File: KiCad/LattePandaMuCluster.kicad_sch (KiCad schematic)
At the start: 0 parts

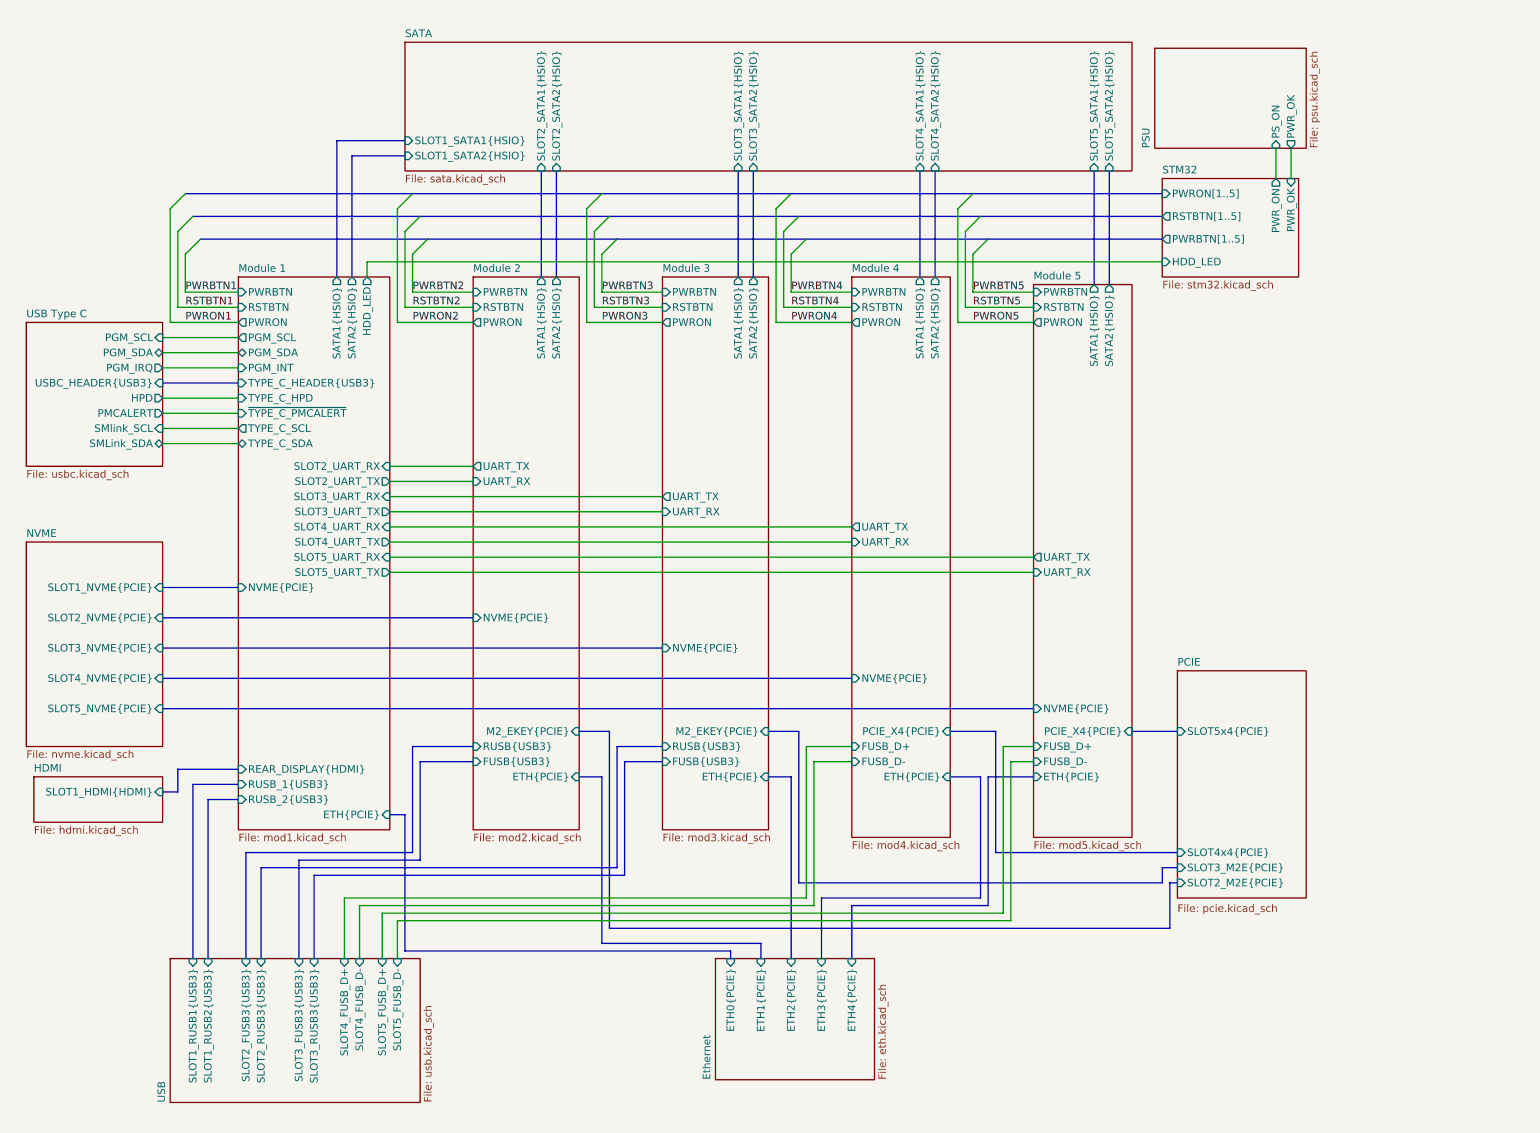
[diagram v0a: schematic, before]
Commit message: Add m.2 slot footprints
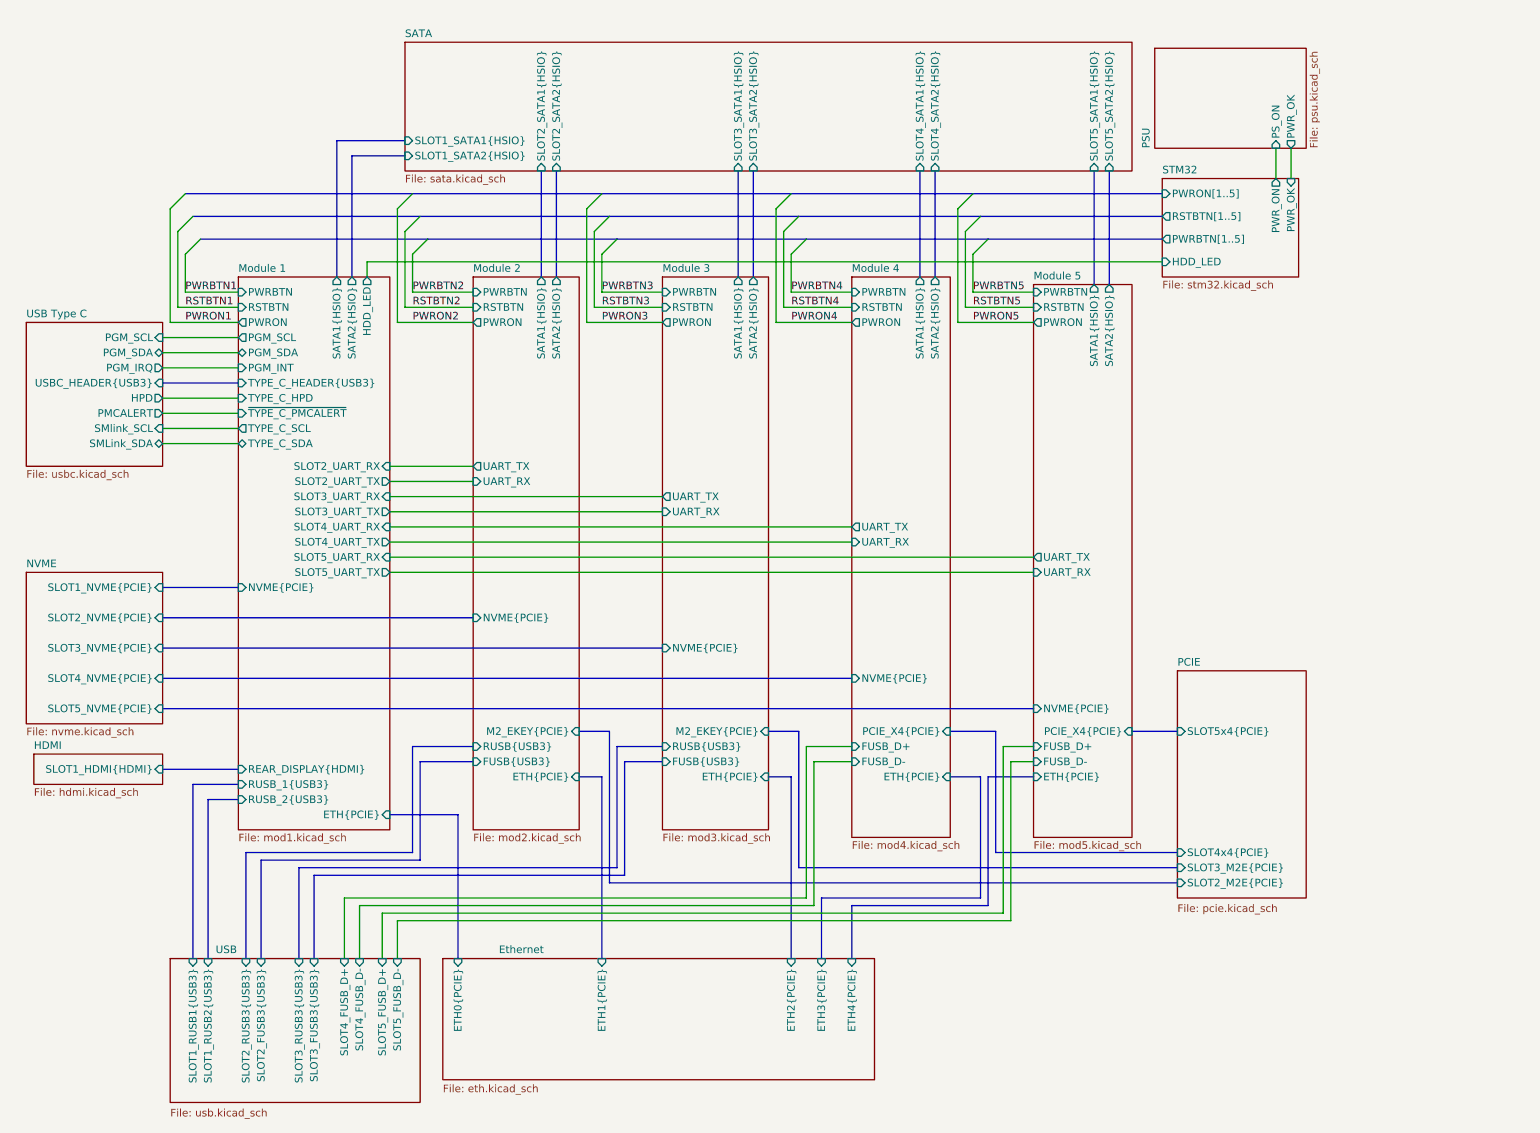
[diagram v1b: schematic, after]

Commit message: Finish fixing footprints
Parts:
- added H1, H2, H3, H4: MountingHole_Pad, MountingHole:MountingHole_4mm_Pad_Via, symbol Mechanical:MountingHole_Pad
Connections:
- new net GND: H1.1, H2.1, H3.1, H4.1

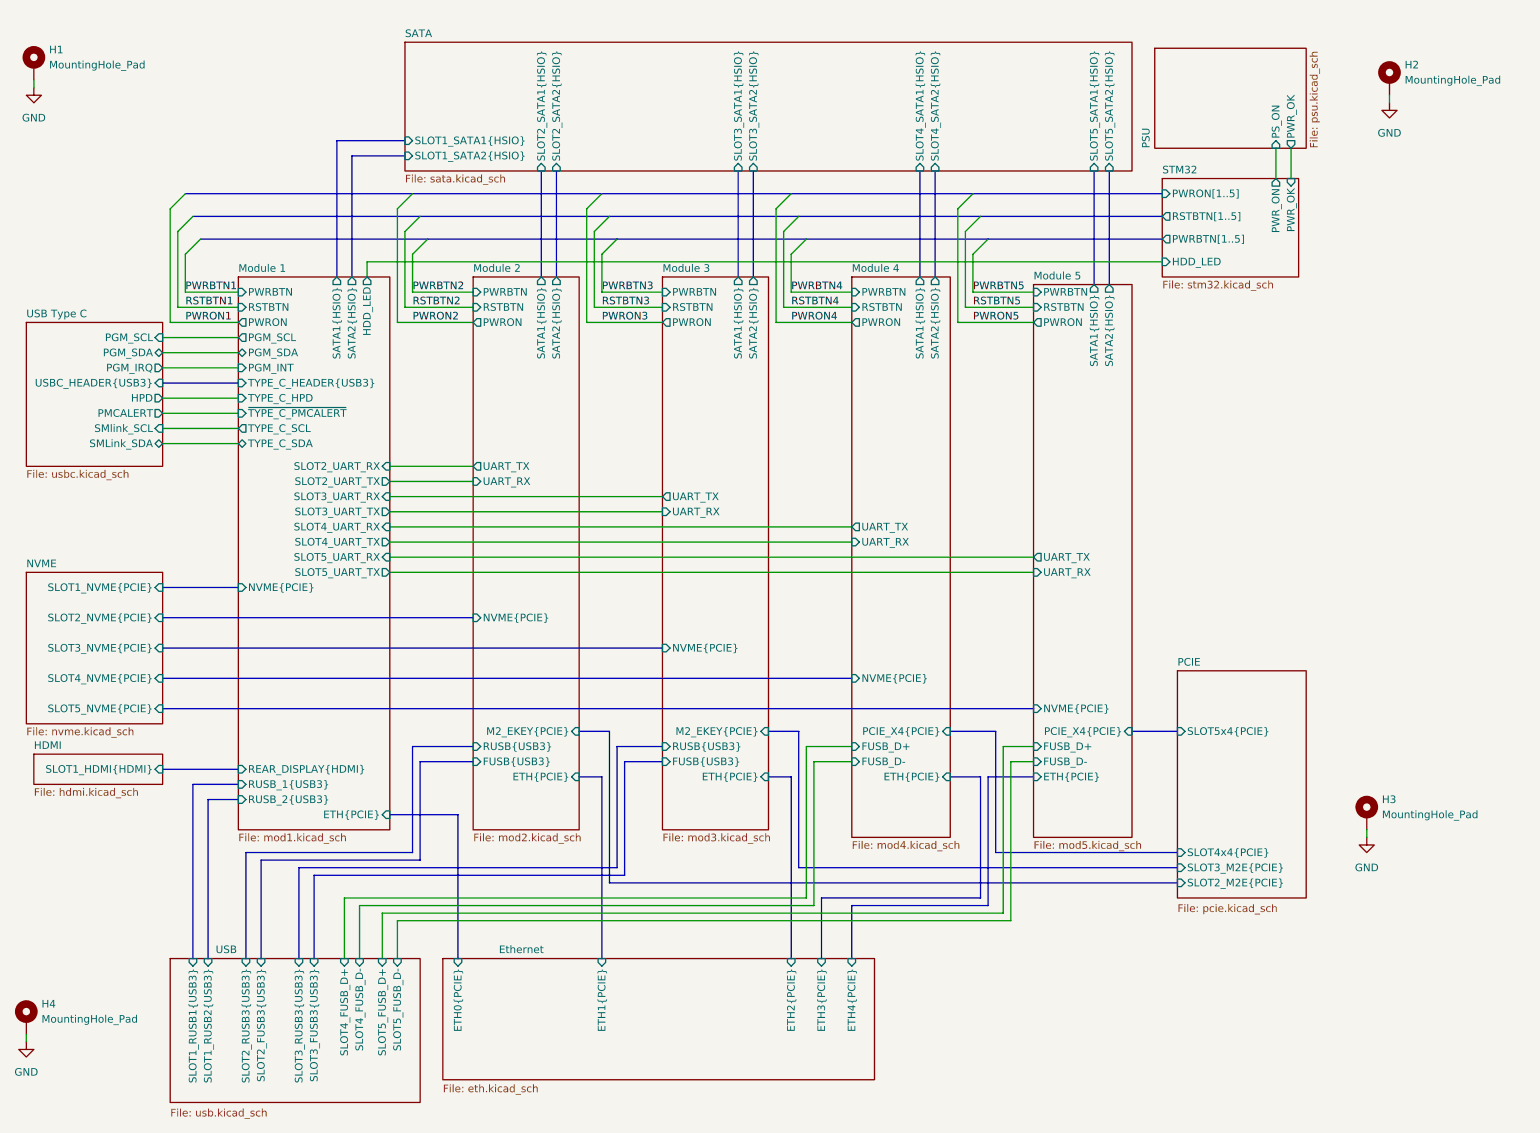
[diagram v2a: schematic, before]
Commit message: Copy modules 2 and 3, remove unnecessary pages
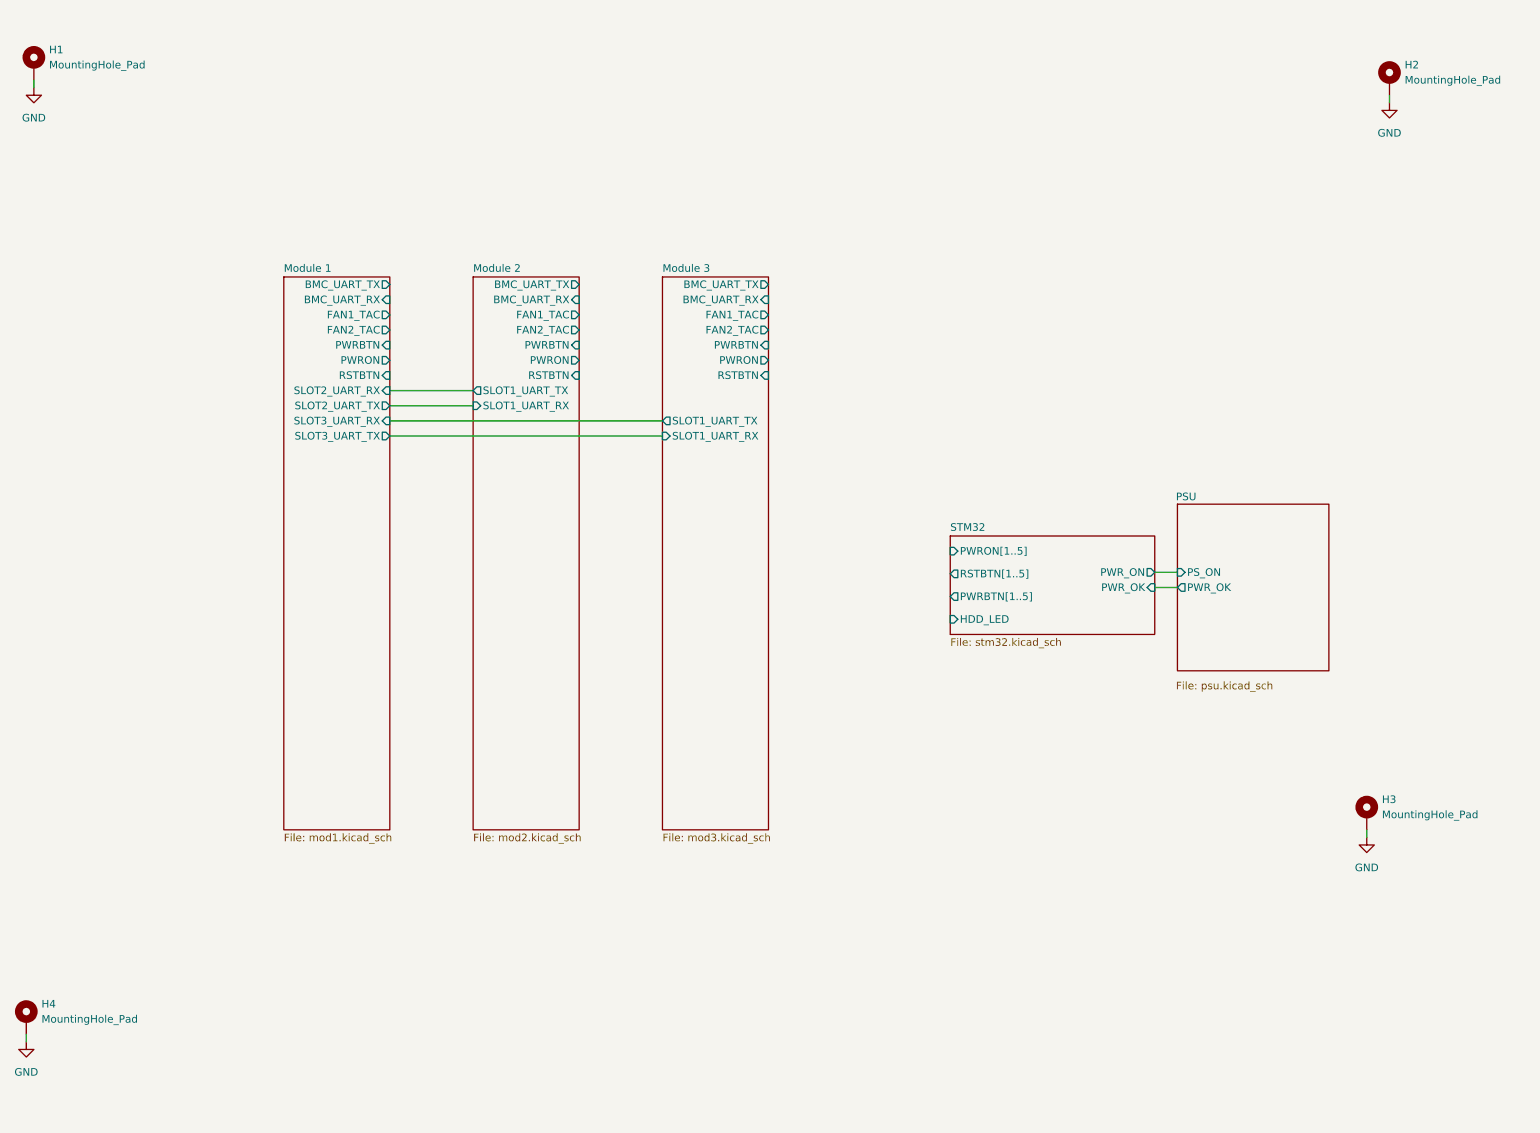
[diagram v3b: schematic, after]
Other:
- removed sheet Ethernet
- removed sheet HDMI
- removed sheet Module 4
- removed sheet Module 5
- removed sheet NVME
- removed sheet PCIE
- removed sheet SATA
- removed sheet USB
- removed sheet USB Type C
- sheet Module 1 ports: added BMC_UART_RX, BMC_UART_TX, FAN1_TAC, FAN2_TAC; removed ETH{PCIE}, HDD_LED, NVME{PCIE}, PGM_INT, PGM_SCL, PGM_SDA, REAR_DISPLAY{HDMI}, RUSB_1{USB3}, RUSB_2{USB3}, SATA1{HSIO}, SATA2{HSIO}, SLOT4_UART_RX, SLOT4_UART_TX, SLOT5_UART_RX, SLOT5_UART_TX, TYPE_C_HEADER{USB3}, TYPE_C_HPD, TYPE_C_SCL, TYPE_C_SDA, ~{TYPE_C_PMCALERT}
- sheet Module 2 ports: added BMC_UART_RX, BMC_UART_TX, FAN1_TAC, FAN2_TAC, SLOT1_UART_RX, SLOT1_UART_TX; removed ETH{PCIE}, FUSB{USB3}, M2_EKEY{PCIE}, NVME{PCIE}, RUSB{USB3}, SATA1{HSIO}, SATA2{HSIO}, UART_RX, UART_TX
- sheet Module 3 ports: added BMC_UART_RX, BMC_UART_TX, FAN1_TAC, FAN2_TAC, SLOT1_UART_RX, SLOT1_UART_TX; removed ETH{PCIE}, FUSB{USB3}, M2_EKEY{PCIE}, NVME{PCIE}, RUSB{USB3}, SATA1{HSIO}, SATA2{HSIO}, UART_RX, UART_TX
